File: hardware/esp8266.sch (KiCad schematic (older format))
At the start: 38 parts

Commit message: Changed atmega power to 3.3v instead of 5v Added type-c connector
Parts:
- removed C? (x2): 100nF, symbol Device:C
- removed U?: TXB0106PWR, Package_SO:TSSOP-16_4.4x5mm_P0.65mm, symbol TXB0106PWR:TXB0106PWR
- Q?: value IRFL024ZTRPBF -> SN7002NH6327; footprint Package_TO_SOT_SMD:SOT-223 -> Package_TO_SOT_SMD:SOT-23
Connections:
- net labels removed: +5V, CLK, CS, MISO, MOSI, RXD, TXD
- wire segments 71 -> 69
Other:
- note removed: "Logical Level Shifter"
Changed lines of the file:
@@
 P 2050 6750
 F 0 "Q?" H 2255 6796 50  0000 L CNN
-F 1 "IRFL024ZTRPBF" H 2255 6705 50  0000 L CNN
-F 2 "Package_TO_SOT_SMD:SOT-223" H 2250 6850 50  0001 C CNN
-F 3 "https://lcsc.com/product-detail/MOSFET_Infineon-Technologies-IRFL024ZTRPBF_C80625.html" H 2050 6750 50  0001 C CNN
+F 1 "SN7002NH6327" H 2255 6705 50  0000 L CNN
+F 2 "Package_TO_SOT_SMD:SOT-23" H 2250 6850 50  0001 C CNN
+F 3 "https://lcsc.com/product-detail/MOSFET_Infineon-Technologies-SN7002NH6327_C151514.html" H 2050 6750 50  0001 C CNN
 	1    2050 6750
 	1    0    0    -1
@@
 Wire Wire Line
 	2150 6400 2050 6400
-Text HLabel 9350 2050 2    50   Output ~ 0
+Text HLabel 6300 3150 2    50   Output ~ 0
 TX
-Text HLabel 9350 1950 2    50   Input ~ 0
+Text HLabel 6300 3050 2    50   Input ~ 0
 RX
 $Comp
@@
 Wire Wire Line
 	6800 3850 6700 3850
-Text HLabel 7950 1950 0    50   Output ~ 0
+Text HLabel 6300 2750 2    50   Output ~ 0
 SPI_MISO
-Text HLabel 7950 1850 0    50   Input ~ 0
+Text HLabel 6300 2650 2    50   Input ~ 0
 SPI_CLK
-Text HLabel 9350 1850 2    50   Input ~ 0
+Text HLabel 6300 2550 2    50   Input ~ 0
 SPI_CS
-Text HLabel 7950 2050 0    50   Input ~ 0
+Text HLabel 6300 3350 2    50   Input ~ 0
 SPI_MOSI
 Wire Wire Line
@@
 Wire Wire Line
 	5650 3550 5700 3550
-$Comp
-L TXB0106PWR:TXB0106PWR U?
-U 1 1 6043CD93
-P 8650 1650
-F 0 "U?" H 8650 2620 50  0000 C CNN
-F 1 "TXB0106PWR" H 8650 2529 50  0000 C CNN
-F 2 "Package_SO:TSSOP-16_4.4x5mm_P0.65mm" H 8650 1650 50  0001 L BNN
-F 3 "" H 8650 1650 50  0001 L BNN
-	1    8650 1650
-	1    0    0    -1
-$EndComp
-$Comp
-L power:+3.3V #PWR0135
-U 1 1 6043FF0E
-P 10350 950
-F 0 "#PWR0135" H 10350 800 50  0001 C CNN
-F 1 "+3.3V" H 10365 1123 50  0000 C CNN
-F 2 "" H 10350 950 50  0001 C CNN
-F 3 "" H 10350 950 50  0001 C CNN
-	1    10350 950
-	1    0    0    -1
-$EndComp
-$Comp
-L power:+5V #PWR0136
-U 1 1 60440060
-P 9900 1050
-F 0 "#PWR0136" H 9900 900 50  0001 C CNN
-F 1 "+5V" H 9915 1223 50  0000 C CNN
-F 2 "" H 9900 1050 50  0001 C CNN
-F 3 "" H 9900 1050 50  0001 C CNN
-	1    9900 1050
-	1    0    0    -1
-$EndComp
-$Comp
-L power:GND #PWR0137
-U 1 1 60442E53
-P 9350 2250
-F 0 "#PWR0137" H 9350 2000 50  0001 C CNN
-F 1 "GND" H 9355 2077 50  0000 C CNN
-F 2 "" H 9350 2250 50  0001 C CNN
-F 3 "" H 9350 2250 50  0001 C CNN
-	1    9350 2250
-	1    0    0    -1
-$EndComp
-$Comp
-L power:+3.3V #PWR0138
-U 1 1 604436ED
-P 7950 1250
-F 0 "#PWR0138" H 7950 1100 50  0001 C CNN
-F 1 "+3.3V" H 7965 1423 50  0000 C CNN
-F 2 "" H 7950 1250 50  0001 C CNN
-F 3 "" H 7950 1250 50  0001 C CNN
-	1    7950 1250
-	1    0    0    -1
-$EndComp
-Text Label 7950 1450 2    50   ~ 0
-CLK
-Text Label 7950 1550 2    50   ~ 0
-MISO
-Text Label 7950 1650 2    50   ~ 0
-MOSI
-Text Label 9350 1450 0    50   ~ 0
-CS
-Text Label 9350 1550 0    50   ~ 0
-RXD
-Text Label 9350 1650 0    50   ~ 0
-TXD
-Text Label 6300 3150 0    50   ~ 0
-TXD
-Text Label 6300 3050 0    50   ~ 0
-RXD
-Text Label 6300 3350 0    50   ~ 0
-MOSI
-Text Label 6300 2750 0    50   ~ 0
-MISO
-Text Label 6300 2650 0    50   ~ 0
-CLK
-Text Label 6300 2550 0    50   ~ 0
-CS
-$Comp
-L Device:C C?
-U 1 1 6046579D
-P 9900 1200
-F 0 "C?" H 10015 1246 50  0000 L CNN
-F 1 "100nF" H 10015 1155 50  0000 L CNN
-F 2 "" H 9938 1050 50  0001 C CNN
-F 3 "~" H 9900 1200 50  0001 C CNN
-	1    9900 1200
-	1    0    0    -1
-$EndComp
-$Comp
-L Device:C C?
-U 1 1 60472470
-P 10350 1100
-F 0 "C?" H 10465 1146 50  0000 L CNN
-F 1 "100nF" H 10465 1055 50  0000 L CNN
-F 2 "" H 10388 950 50  0001 C CNN
-F 3 "~" H 10350 1100 50  0001 C CNN
-	1    10350 1100
-	1    0    0    -1
-$EndComp
-Wire Wire Line
-	9350 950  10350 950
-Connection ~ 10350 950
-Wire Wire Line
-	9350 1050 9900 1050
-Connection ~ 9900 1050
-$Comp
-L power:GND #PWR0139
-U 1 1 6047798E
-P 9900 1350
-F 0 "#PWR0139" H 9900 1100 50  0001 C CNN
-F 1 "GND" H 9905 1177 50  0000 C CNN
-F 2 "" H 9900 1350 50  0001 C CNN
-F 3 "" H 9900 1350 50  0001 C CNN
-	1    9900 1350
-	1    0    0    -1
-$EndComp
-$Comp
-L power:GND #PWR0140
-U 1 1 604787D4
-P 10350 1250
-F 0 "#PWR0140" H 10350 1000 50  0001 C CNN
-F 1 "GND" H 10355 1077 50  0000 C CNN
-F 2 "" H 10350 1250 50  0001 C CNN
-F 3 "" H 10350 1250 50  0001 C CNN
-	1    10350 1250
-	1    0    0    -1
-$EndComp
-Text Notes 8300 2550 0    50   ~ 0
-Logical Level Shifter
 $EndSCHEMATC

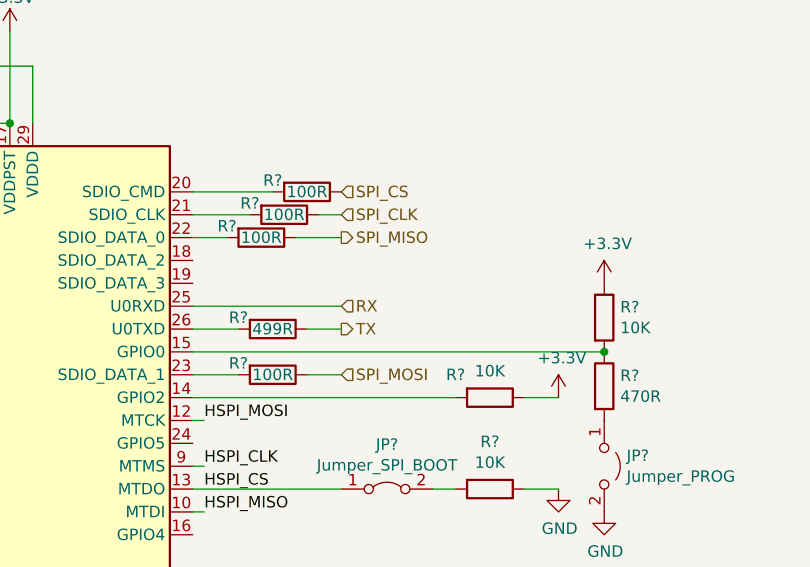
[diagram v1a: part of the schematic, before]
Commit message: Finished routing USB type-c and battery charging IC
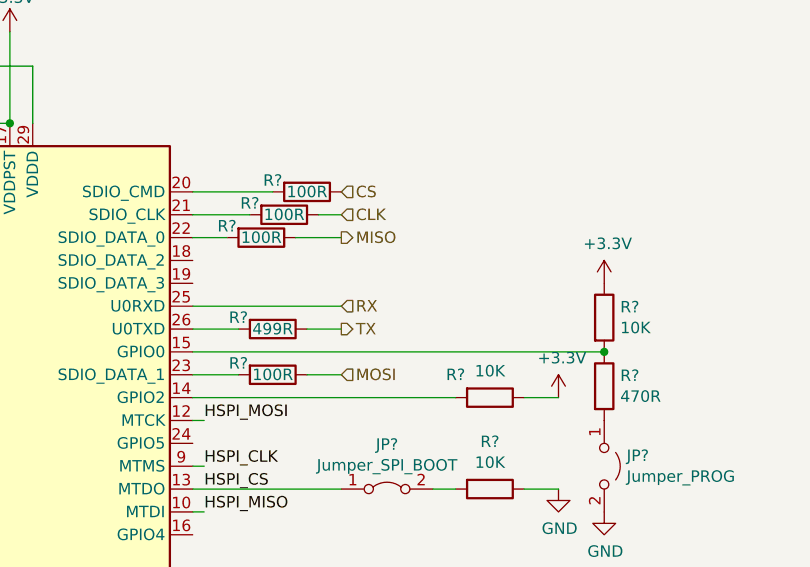
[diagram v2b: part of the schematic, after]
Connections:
- net labels added: CLK, CS, MISO, MOSI
- net labels removed: SPI_CLK, SPI_CS, SPI_MISO, SPI_MOSI
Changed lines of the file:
@@
 	6800 3850 6700 3850
 Text HLabel 6300 2750 2    50   Output ~ 0
-SPI_MISO
+MISO
 Text HLabel 6300 2650 2    50   Input ~ 0
-SPI_CLK
+CLK
 Text HLabel 6300 2550 2    50   Input ~ 0
-SPI_CS
+CS
 Text HLabel 6300 3350 2    50   Input ~ 0
-SPI_MOSI
+MOSI
 Wire Wire Line
 	5650 3450 6800 3450

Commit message: Changed flash for esp8266 Added stm32 schematic
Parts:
- removed JP?: Jumper_SPI_BOOT, symbol Jumper:Jumper_2_Bridged
- removed R?: 470R, symbol Device:R
- removed R? (x2): 10K, symbol Device:R
- removed R?: 50R, symbol Device:R
- removed U?: AT45DB041E-SSHN-B, Package_SO:SOIC-8_5.275x5.275mm_P1.27mm, symbol Memory_Flash:AT45DB161D-SU
- added C?: 100nF, symbol Device:C
- added R? (x2): 10K, symbol Device:R
- added R? (x4): 100R, symbol Device:R
- added U?: AT25SF081-SHD-T, symbol Memory_EEPROM:AT25xxx
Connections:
- wire segments 69 -> 72
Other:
- moved on the sheet: JP?, R?

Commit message: Finished power schematics
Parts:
- removed C?: 100nF, symbol Device:C
- removed Q?: SN7002NH6327, Package_TO_SOT_SMD:SOT-23, symbol Device:Q_NMOS_GDS
- removed R?: 10K, symbol Device:R
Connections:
- wire segments 72 -> 67
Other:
- moved on the sheet: R?
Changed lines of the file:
@@
 $Descr A4 11693 8268
 encoding utf-8
-Sheet 2 3
+Sheet 2 4
 Title ""
 Date ""
@@
 L Device:R R?
 U 1 1 60338D72
-P 2150 6250
-F 0 "R?" H 2080 6204 50  0000 R CNN
-F 1 "10K" H 2080 6295 50  0000 R CNN
-F 2 "" V 2080 6250 50  0001 C CNN
-F 3 "~" H 2150 6250 50  0001 C CNN
-	1    2150 6250
+P 2100 1650
+F 0 "R?" H 2030 1604 50  0000 R CNN
+F 1 "10K" H 2030 1695 50  0000 R CNN
+F 2 "" V 2030 1650 50  0001 C CNN
+F 3 "~" H 2100 1650 50  0001 C CNN
+	1    2100 1650
 	-1   0    0    1
 $EndComp
@@
 L power:+3.3V #PWR0123
 U 1 1 6033B326
-P 2150 6100
-F 0 "#PWR0123" H 2150 5950 50  0001 C CNN
-F 1 "+3.3V" H 2165 6273 50  0000 C CNN
-F 2 "" H 2150 6100 50  0001 C CNN
-F 3 "" H 2150 6100 50  0001 C CNN
-	1    2150 6100
-	1    0    0    -1
-$EndComp
-$Comp
-L power:GND #PWR0124
-U 1 1 6035AA4B
-P 2150 7150
-F 0 "#PWR0124" H 2150 6900 50  0001 C CNN
-F 1 "GND" H 2155 6977 50  0000 C CNN
-F 2 "" H 2150 7150 50  0001 C CNN
-F 3 "" H 2150 7150 50  0001 C CNN
-	1    2150 7150
-	1    0    0    -1
-$EndComp
-Text HLabel 1350 6750 0    50   Input ~ 0
+P 2100 1500
+F 0 "#PWR0123" H 2100 1350 50  0001 C CNN
+F 1 "+3.3V" H 2115 1673 50  0000 C CNN
+F 2 "" H 2100 1500 50  0001 C CNN
+F 3 "" H 2100 1500 50  0001 C CNN
+	1    2100 1500
+	1    0    0    -1
+$EndComp
+Text HLabel 1600 1900 0    50   Input ~ 0
 CHIP_DISABLE
 $Comp
 L Device:R R?
-U 1 1 6035C3FF
-P 1750 7000
-F 0 "R?" H 1680 6954 50  0000 R CNN
-F 1 "10K" H 1680 7045 50  0000 R CNN
-F 2 "" V 1680 7000 50  0001 C CNN
-F 3 "~" H 1750 7000 50  0001 C CNN
-	1    1750 7000
-	-1   0    0    1
-$EndComp
-$Comp
-L Device:R R?
 U 1 1 6035E947
-P 1500 6750
-F 0 "R?" V 1293 6750 50  0000 C CNN
-F 1 "220R" V 1384 6750 50  0000 C CNN
-F 2 "" V 1430 6750 50  0001 C CNN
-F 3 "~" H 1500 6750 50  0001 C CNN
-	1    1500 6750
-	0    1    1    0
-$EndComp
-Wire Wire Line
-	1750 7150 2150 7150
-Wire Wire Line
-	2150 6950 2150 7150
-Connection ~ 2150 7150
-Wire Wire Line
-	1650 6750 1750 6750
-Wire Wire Line
-	1750 6850 1750 6750
-Connection ~ 1750 6750
-Wire Wire Line
-	1750 6750 1850 6750
+P 1750 1900
+F 0 "R?" V 1543 1900 50  0000 C CNN
+F 1 "220R" V 1634 1900 50  0000 C CNN
+F 2 "" V 1680 1900 50  0001 C CNN
+F 3 "~" H 1750 1900 50  0001 C CNN
+	1    1750 1900
+	0    1    1    0
+$EndComp
 Text Label 3500 2850 0    50   ~ 0
 CHIP_PU
 Wire Wire Line
 	3500 2850 3850 2850
-Text Label 2400 6400 0    50   ~ 0
+Text Label 2450 1900 0    50   ~ 0
 CHIP_PU
-$Comp
-L Device:Q_NMOS_GDS Q?
-U 1 1 60374F0D
-P 2050 6750
-F 0 "Q?" H 2255 6796 50  0000 L CNN
-F 1 "SN7002NH6327" H 2255 6705 50  0000 L CNN
-F 2 "Package_TO_SOT_SMD:SOT-23" H 2250 6850 50  0001 C CNN
-F 3 "https://lcsc.com/product-detail/MOSFET_Infineon-Technologies-SN7002NH6327_C151514.html" H 2050 6750 50  0001 C CNN
-	1    2050 6750
-	1    0    0    -1
-$EndComp
-$Comp
-L Device:C C?
-U 1 1 6034AC2C
-P 1900 6400
-F 0 "C?" V 1648 6400 50  0000 C CNN
-F 1 "100nF" V 1739 6400 50  0000 C CNN
-F 2 "" H 1938 6250 50  0001 C CNN
-F 3 "~" H 1900 6400 50  0001 C CNN
-	1    1900 6400
-	0    1    1    0
-$EndComp
-$Comp
-L power:GND #PWR0125
-U 1 1 6034CB2C
-P 1750 6400
-F 0 "#PWR0125" H 1750 6150 50  0001 C CNN
-F 1 "GND" H 1755 6227 50  0000 C CNN
-F 2 "" H 1750 6400 50  0001 C CNN
-F 3 "" H 1750 6400 50  0001 C CNN
-	1    1750 6400
-	1    0    0    -1
-$EndComp
-Wire Wire Line
-	2150 6550 2150 6400
-Wire Wire Line
-	2400 6400 2150 6400
-Connection ~ 2150 6400
-Wire Wire Line
-	2150 6400 2050 6400
 Text HLabel 6300 3150 2    50   Output ~ 0
 TX
@@
 $EndComp
 $Comp
-L power:GND #PWR?
+L power:GND #PWR0104
 U 1 1 60490DA8
 P 9600 6050
-F 0 "#PWR?" H 9600 5800 50  0001 C CNN
+F 0 "#PWR0104" H 9600 5800 50  0001 C CNN
 F 1 "GND" H 9605 5877 50  0000 C CNN
 F 2 "" H 9600 6050 50  0001 C CNN
@@
 $EndComp
 $Comp
-L power:+3.3V #PWR?
+L power:+3.3V #PWR0105
 U 1 1 60491A11
 P 9600 5450
-F 0 "#PWR?" H 9600 5300 50  0001 C CNN
+F 0 "#PWR0105" H 9600 5300 50  0001 C CNN
 F 1 "+3.3V" H 9615 5623 50  0000 C CNN
 F 2 "" H 9600 5450 50  0001 C CNN
@@
 $EndComp
 $Comp
-L power:+3.3V #PWR?
+L power:+3.3V #PWR0106
 U 1 1 60494A10
 P 7400 5550
-F 0 "#PWR?" H 7400 5400 50  0001 C CNN
+F 0 "#PWR0106" H 7400 5400 50  0001 C CNN
 F 1 "+3.3V" H 7415 5723 50  0000 C CNN
 F 2 "" H 7400 5550 50  0001 C CNN
@@
 $EndComp
 $Comp
-L power:GND #PWR?
+L power:GND #PWR0109
 U 1 1 60495448
 P 7400 5850
-F 0 "#PWR?" H 7400 5600 50  0001 C CNN
+F 0 "#PWR0109" H 7400 5600 50  0001 C CNN
 F 1 "GND" H 7405 5677 50  0000 C CNN
 F 2 "" H 7400 5850 50  0001 C CNN
@@
 	9200 5650 8450 5650
 $Comp
-L power:+3.3V #PWR?
+L power:+3.3V #PWR0110
 U 1 1 604B5C7D
 P 7950 5650
-F 0 "#PWR?" H 7950 5500 50  0001 C CNN
+F 0 "#PWR0110" H 7950 5500 50  0001 C CNN
 F 1 "+3.3V" H 7965 5823 50  0000 C CNN
 F 2 "" H 7950 5650 50  0001 C CNN
@@
 Wire Wire Line
 	6950 3550 7100 3550
+Wire Wire Line
+	2100 1800 2100 1900
+Wire Wire Line
+	1900 1900 2100 1900
+Connection ~ 2100 1900
+Wire Wire Line
+	2100 1900 2450 1900
 $EndSCHEMATC

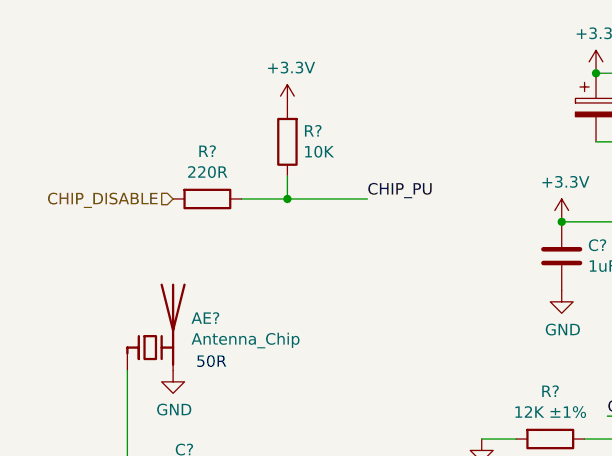
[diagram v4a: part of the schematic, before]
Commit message: All sensors + most of MCU done
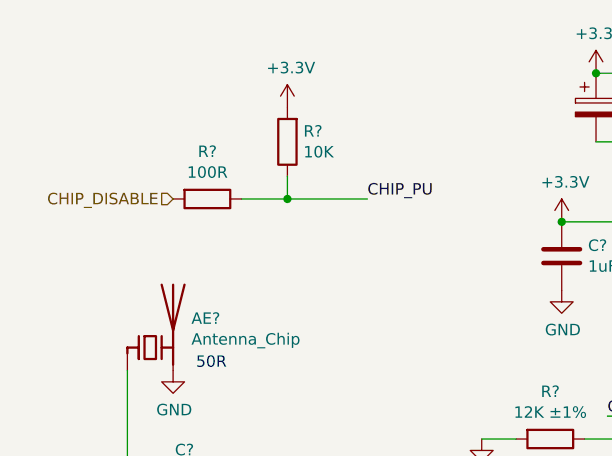
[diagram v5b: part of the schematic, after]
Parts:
- R?: value 220R -> 100R
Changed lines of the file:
@@
 $Descr A4 11693 8268
 encoding utf-8
-Sheet 2 4
+Sheet 2 5
 Title ""
 Date ""
@@
 P 1750 1900
 F 0 "R?" V 1543 1900 50  0000 C CNN
-F 1 "220R" V 1634 1900 50  0000 C CNN
+F 1 "100R" V 1634 1900 50  0000 C CNN
 F 2 "" V 1680 1900 50  0001 C CNN
 F 3 "~" H 1750 1900 50  0001 C CNN

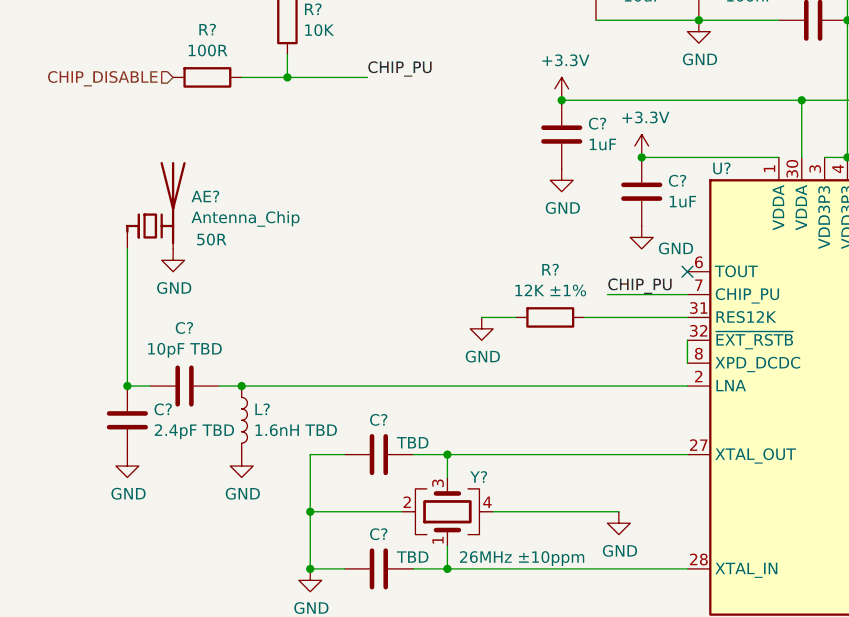
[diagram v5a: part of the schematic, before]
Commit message: Finished sx1278 schematic
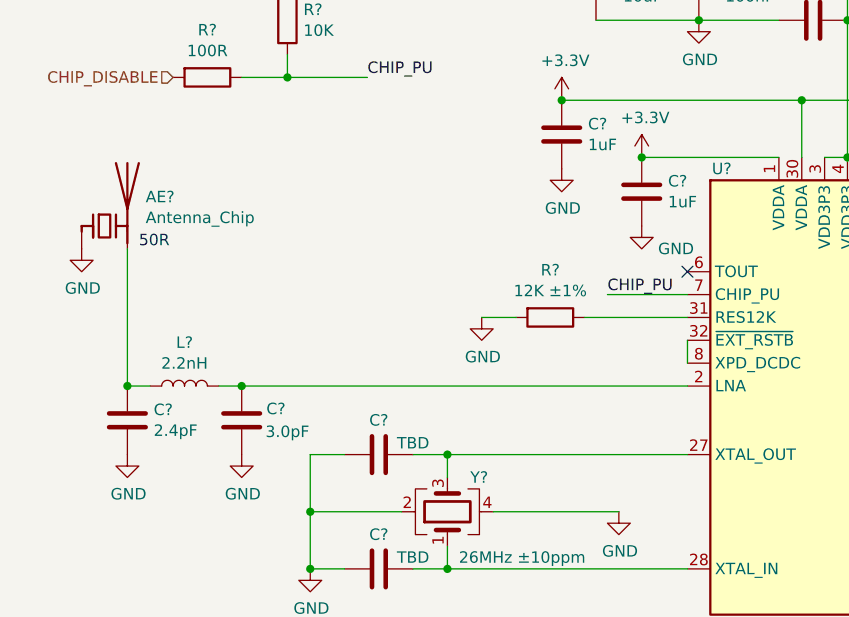
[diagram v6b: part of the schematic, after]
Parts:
- removed L?: 1.6nH TBD, symbol Device:L
- added L?: 2.2nH, symbol Device:L
- C?: value 10pF TBD -> 3.0pF
- C?: value 2.4pF TBD -> 2.4pF
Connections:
- net GND: now also AE?.1 (FEED), C?.1; no longer AE?.2 (PCB_Trace)
- net at U?.2 (LNA): now also C?.2, L?.2; no longer C?.1
- new net: AE?.2 (PCB_Trace), C?.2, L?.1
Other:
- moved on the sheet: AE?, C?
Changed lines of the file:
@@
 	3850 3150 3850 3050
 $Comp
-L Device:L L?
-U 1 1 60354012
+L Device:C C?
+U 1 1 6035839E
 P 1900 3400
-F 0 "L?" H 1953 3446 50  0000 L CNN
-F 1 "1.6nH TBD" H 1953 3355 50  0000 L CNN
-F 2 "" H 1900 3400 50  0001 C CNN
+F 0 "C?" H 1750 3350 50  0000 C CNN
+F 1 "3.0pF" H 1700 3450 50  0000 C CNN
+F 2 "" H 1938 3250 50  0001 C CNN
 F 3 "~" H 1900 3400 50  0001 C CNN
 	1    1900 3400
-	1    0    0    -1
-$EndComp
-Wire Wire Line
-	3850 3250 1900 3250
-$Comp
-L Device:C C?
-U 1 1 6035839E
-P 1650 3250
-F 0 "C?" V 1398 3250 50  0000 C CNN
-F 1 "10pF TBD" V 1489 3250 50  0000 C CNN
-F 2 "" H 1688 3100 50  0001 C CNN
-F 3 "~" H 1650 3250 50  0001 C CNN
-	1    1650 3250
-	0    1    1    0
+	-1   0    0    1
 $EndComp
 $Comp
@@
 P 1400 3400
 F 0 "C?" H 1285 3354 50  0000 R CNN
-F 1 "2.4pF TBD" H 1285 3445 50  0000 R CNN
+F 1 "2.4pF" H 1285 3445 50  0000 R CNN
 F 2 "" H 1438 3250 50  0001 C CNN
 F 3 "~" H 1400 3400 50  0001 C CNN
@@
 	1400 3250 1500 3250
 Wire Wire Line
-	1800 3250 1900 3250
-Connection ~ 1900 3250
-$Comp
-L Device:Antenna_Chip AE?
-U 1 1 6035FFB8
-P 1500 2550
-F 0 "AE?" H 1680 2677 50  0000 L CNN
-F 1 "Antenna_Chip" H 1680 2586 50  0000 L CNN
-F 2 "Connector_Coaxial:SMA_Molex_73251-2200_Horizontal" H 1400 2725 50  0001 C CNN
-F 3 "~" H 1400 2725 50  0001 C CNN
-	1    1500 2550
-	1    0    0    -1
-$EndComp
-$Comp
-L power:GND #PWR0128
-U 1 1 60369B3C
-P 1600 2650
-F 0 "#PWR0128" H 1600 2400 50  0001 C CNN
-F 1 "GND" H 1605 2477 50  0000 C CNN
-F 2 "" H 1600 2650 50  0001 C CNN
-F 3 "" H 1600 2650 50  0001 C CNN
-	1    1600 2650
-	1    0    0    -1
-$EndComp
-Wire Wire Line
 	1400 2650 1400 3250
 Connection ~ 1400 3250
@@
 Wire Wire Line
 	6500 3850 6650 3850
-Text Notes 1700 2650 0    50   ~ 0
-50R
 Wire Wire Line
 	5650 3250 7450 3250
@@
 Wire Wire Line
 	2100 1900 2450 1900
+Text Notes 1450 2650 0    50   ~ 0
+50R
+$Comp
+L power:GND #PWR0128
+U 1 1 60369B3C
+P 1200 2650
+F 0 "#PWR0128" H 1200 2400 50  0001 C CNN
+F 1 "GND" H 1205 2477 50  0000 C CNN
+F 2 "" H 1200 2650 50  0001 C CNN
+F 3 "" H 1200 2650 50  0001 C CNN
+	1    1200 2650
+	1    0    0    -1
+$EndComp
+$Comp
+L Device:Antenna_Chip AE?
+U 1 1 6035FFB8
+P 1300 2550
+F 0 "AE?" H 1480 2677 50  0000 L CNN
+F 1 "Antenna_Chip" H 1480 2586 50  0000 L CNN
+F 2 "Connector_Coaxial:SMA_Molex_73251-2200_Horizontal" H 1200 2725 50  0001 C CNN
+F 3 "~" H 1200 2725 50  0001 C CNN
+	1    1300 2550
+	1    0    0    -1
+$EndComp
+Wire Wire Line
+	1800 3250 1900 3250
+$Comp
+L Device:L L?
+U 1 1 60A29D12
+P 1650 3250
+F 0 "L?" V 1840 3250 50  0000 C CNN
+F 1 "2.2nH" V 1749 3250 50  0000 C CNN
+F 2 "" H 1650 3250 50  0001 C CNN
+F 3 "~" H 1650 3250 50  0001 C CNN
+	1    1650 3250
+	0    -1   -1   0
+$EndComp
+Connection ~ 1900 3250
+Wire Wire Line
+	1900 3250 3850 3250
 $EndSCHEMATC
